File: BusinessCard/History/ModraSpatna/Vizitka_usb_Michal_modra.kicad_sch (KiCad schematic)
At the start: 29 parts, among them J1 USB_B_Micro, J2 USB_C_Receptacle, J3 Conn_01x01

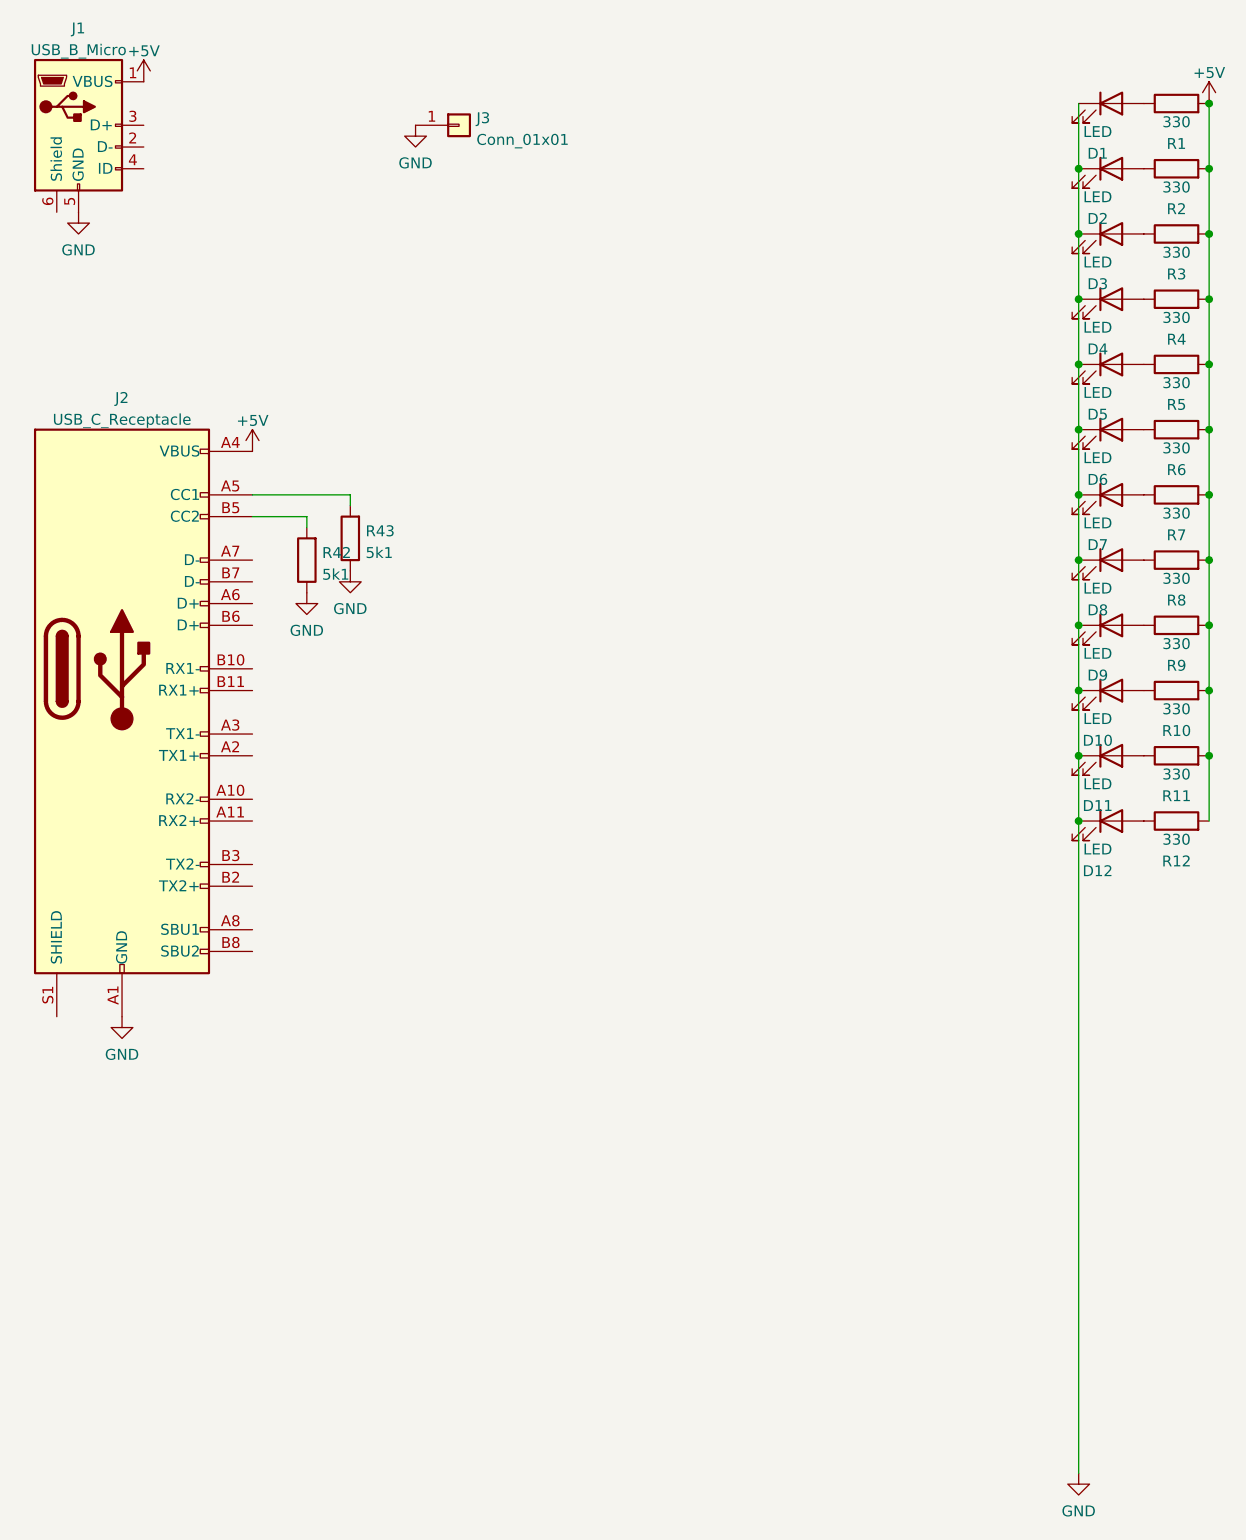
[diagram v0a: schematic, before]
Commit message: Added aditional businesscards - Zuza, MichalModra...Actual Tapeout 2023-08-24, but repaired connection!
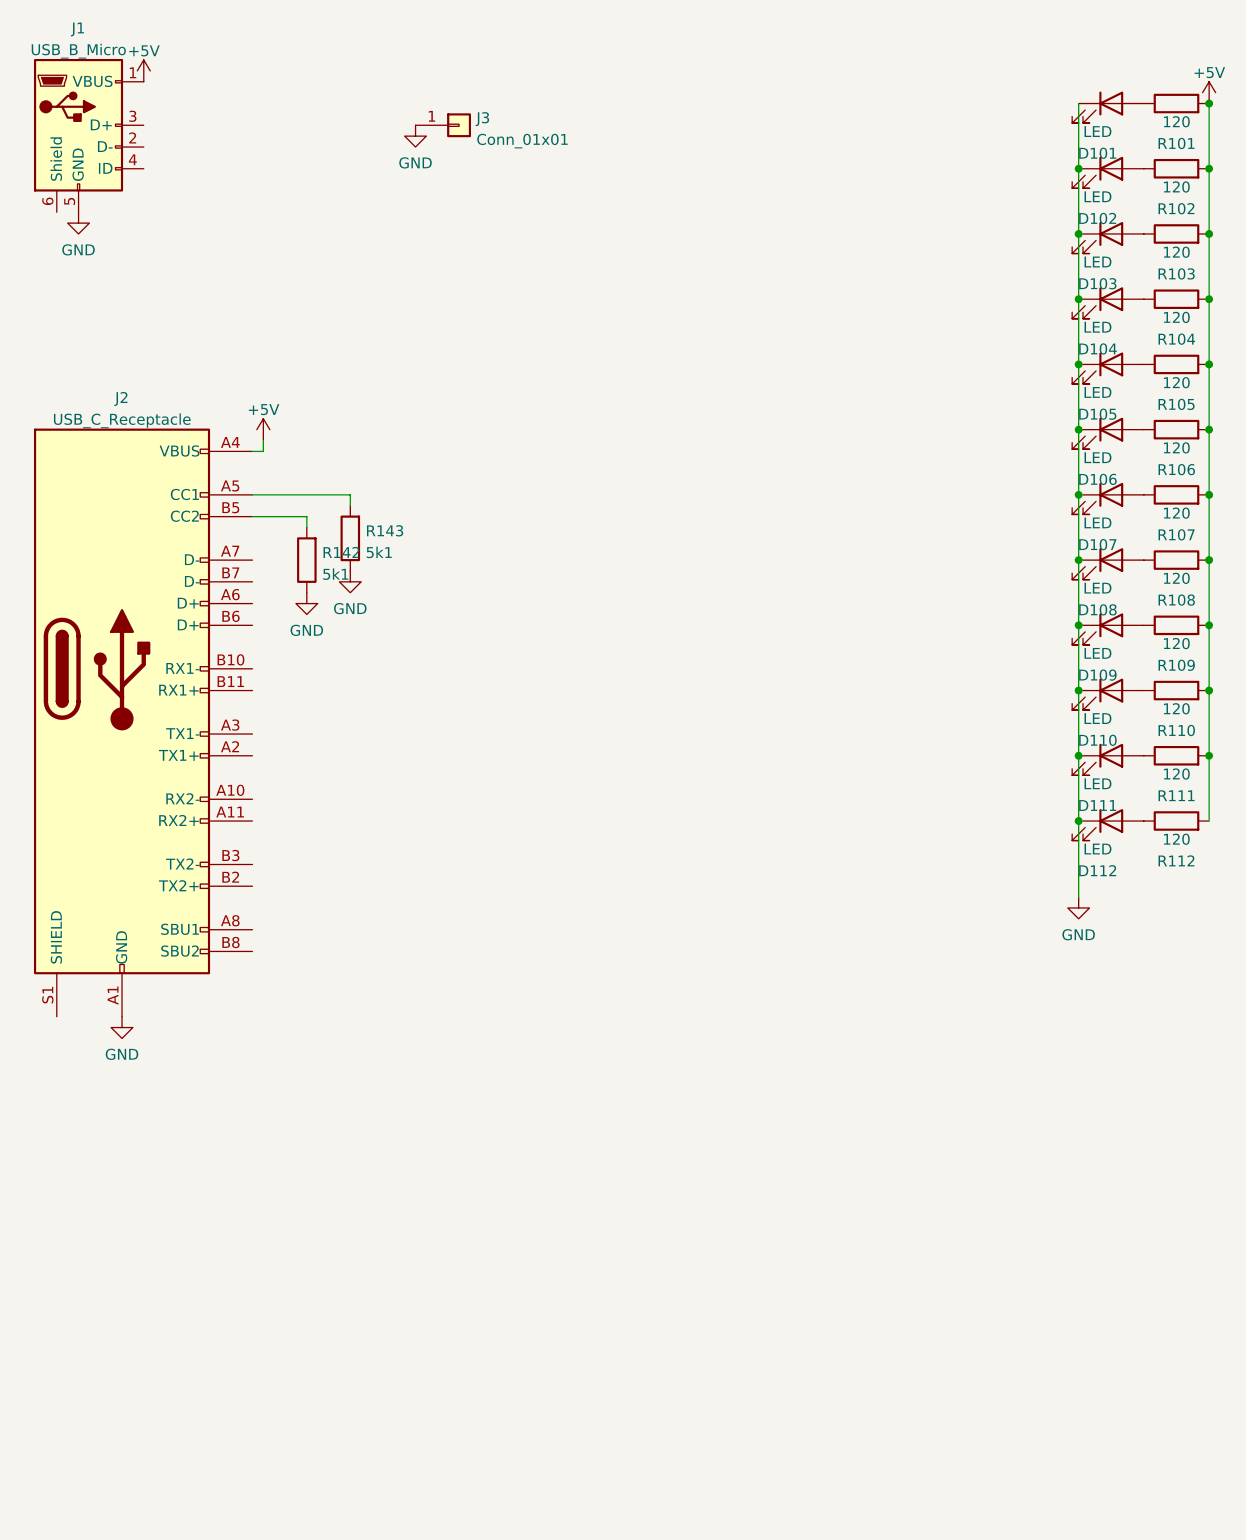
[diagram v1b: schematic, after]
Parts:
- D101: renamed from D1; footprint meteopress:D_0802_side_woSilk -> meteopress:D_0802_side_woSilk_C965872; LCSC C2827268 -> C965872
- D102: renamed from D2; footprint meteopress:D_0802_side_woSilk -> meteopress:D_0802_side_woSilk_C965872; LCSC C2827268 -> C965872
- D103: renamed from D3; footprint meteopress:D_0802_side_woSilk -> meteopress:D_0802_side_woSilk_C965872; LCSC C2827268 -> C965872
- D104: renamed from D4; footprint meteopress:D_0802_side_woSilk -> meteopress:D_0802_side_woSilk_C965872; LCSC C2827268 -> C965872
- D105: renamed from D5; footprint meteopress:D_0802_side_woSilk -> meteopress:D_0802_side_woSilk_C965872; LCSC C2827268 -> C965872
- D106: renamed from D6; footprint meteopress:D_0802_side_woSilk -> meteopress:D_0802_side_woSilk_C965872; LCSC C2827268 -> C965872
- D107: renamed from D7; footprint meteopress:D_0802_side_woSilk -> meteopress:D_0802_side_woSilk_C965872; LCSC C2827268 -> C965872
- D108: renamed from D8; footprint meteopress:D_0802_side_woSilk -> meteopress:D_0802_side_woSilk_C965872; LCSC C2827268 -> C965872
- D109: renamed from D9; footprint meteopress:D_0802_side_woSilk -> meteopress:D_0802_side_woSilk_C965872; LCSC C2827268 -> C965872
- D110: renamed from D10; footprint meteopress:D_0802_side_woSilk -> meteopress:D_0802_side_woSilk_C965872; LCSC C2827268 -> C965872
- D111: renamed from D11; footprint meteopress:D_0802_side_woSilk -> meteopress:D_0802_side_woSilk_C965872; LCSC C2827268 -> C965872
- D112: renamed from D12; footprint meteopress:D_0802_side_woSilk -> meteopress:D_0802_side_woSilk_C965872; LCSC C2827268 -> C965872
- R101: renamed from R1; value 330 -> 120; LCSC C473445 -> C226406
- R102: renamed from R2; value 330 -> 120; LCSC C473445 -> C226406
- R103: renamed from R3; value 330 -> 120; LCSC C473445 -> C226406
- R104: renamed from R4; value 330 -> 120; LCSC C473445 -> C226406
- R105: renamed from R5; value 330 -> 120; LCSC C473445 -> C226406
- R106: renamed from R6; value 330 -> 120; LCSC C473445 -> C226406
- R107: renamed from R7; value 330 -> 120; LCSC C473445 -> C226406
- R108: renamed from R8; value 330 -> 120; LCSC C473445 -> C226406
- R109: renamed from R9; value 330 -> 120; LCSC C473445 -> C226406
- R110: renamed from R10; value 330 -> 120; LCSC C473445 -> C226406
- R111: renamed from R11; value 330 -> 120; LCSC C473445 -> C226406
- R112: renamed from R12; value 330 -> 120; LCSC C473445 -> C226406
- renumbered R42 to R142, R43 to R143
